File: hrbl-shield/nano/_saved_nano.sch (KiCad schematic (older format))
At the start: 78 parts, among them P1 Digital, P2 Analog, U1 SFH6206-3T, U10 SFH6206-3T, U11 SFH6206-3T, U12 SFH6206-3T, U13 SFH6206-3T, U14 SFH6206-3T, U15 IFX27001TFV50ATMA1CT-ND, U16 SFH6206-3T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

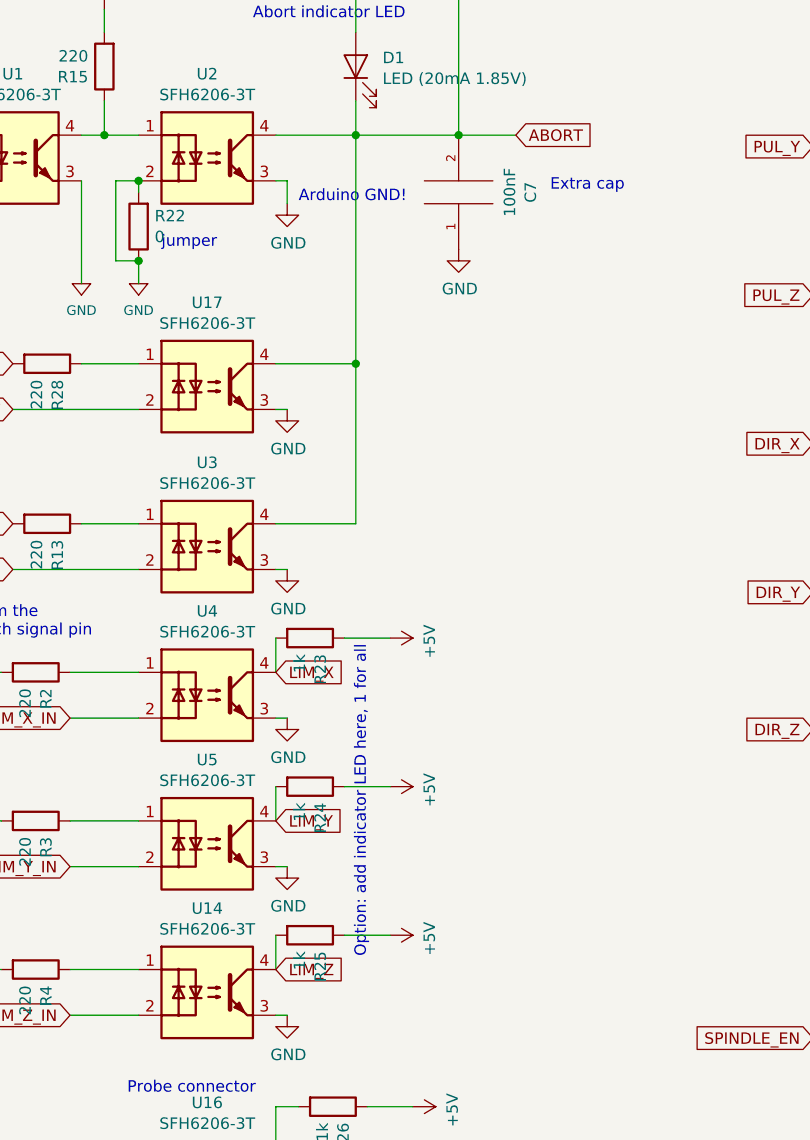
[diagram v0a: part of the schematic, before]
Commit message: Added serial pins and more noise protection
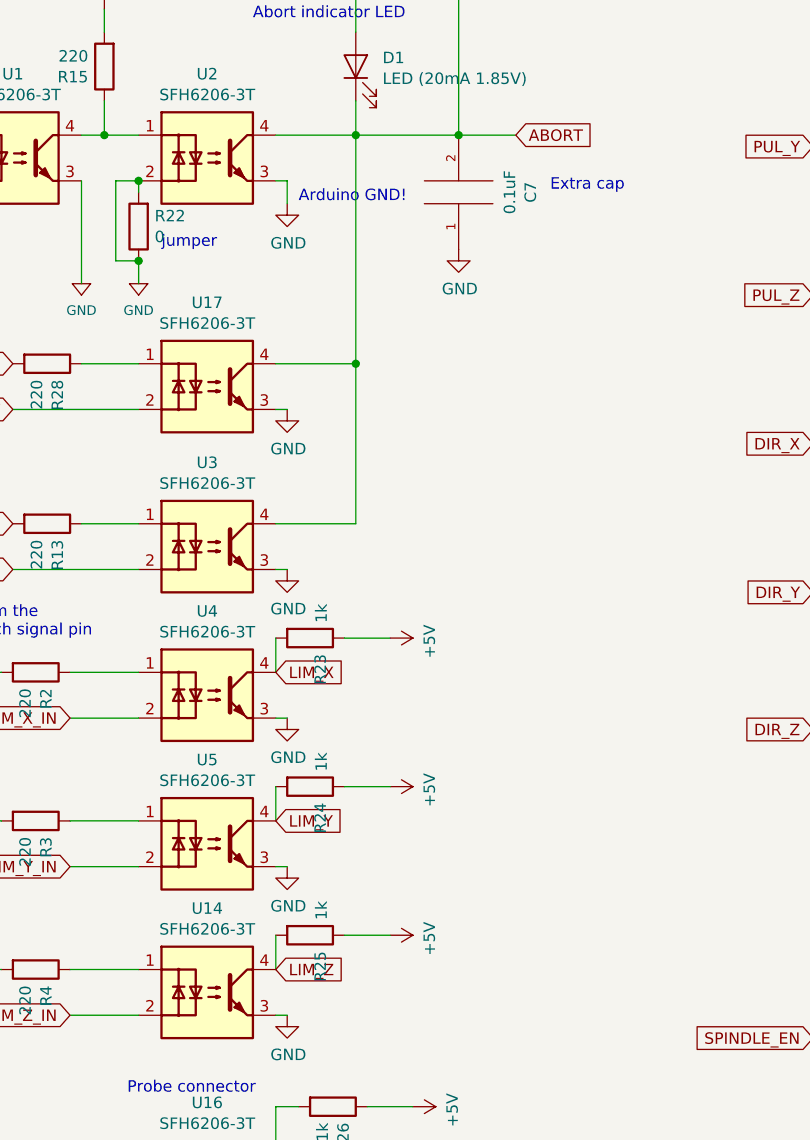
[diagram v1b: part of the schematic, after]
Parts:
- C7: value 100nF -> 0.1uF
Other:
- note removed: "Option: add indicator LED here, 1 for all"
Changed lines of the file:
@@
 PROBE
 $Bitmap
-Pos 11750 1650
+Pos 8300 2400
 Scale 1.000000
 Data
@@
 P 2500 5050
 F 0 "R25" H 2570 5096 50  0000 L CNN
-F 1 "1k" H 2570 5005 50  0000 L CNN
+F 1 "1k" H 2350 5100 50  0000 L CNN
 F 2 "Resistor_SMD:R_1206_3216Metric_Pad1.42x1.75mm_HandSolder" V 2430 5050 50  0001 C CNN
 F 3 "~" H 2500 5050 50  0001 C CNN
@@
 P 2500 4400
 F 0 "R24" H 2570 4446 50  0000 L CNN
-F 1 "1k" H 2570 4355 50  0000 L CNN
+F 1 "1k" H 2350 4450 50  0000 L CNN
 F 2 "Resistor_SMD:R_1206_3216Metric_Pad1.42x1.75mm_HandSolder" V 2430 4400 50  0001 C CNN
 F 3 "~" H 2500 4400 50  0001 C CNN
@@
 P 2500 3750
 F 0 "R23" H 2570 3796 50  0000 L CNN
-F 1 "1k" H 2570 3705 50  0000 L CNN
+F 1 "1k" H 2350 3800 50  0000 L CNN
 F 2 "Resistor_SMD:R_1206_3216Metric_Pad1.42x1.75mm_HandSolder" V 2430 3750 50  0001 C CNN
 F 3 "~" H 2500 3750 50  0001 C CNN
@@
 Wire Wire Line
 	13850 8800 14000 8800
-Text Notes 2750 5150 1    50   ~ 0
-Option: add indicator LED here, 1 for all
 Text Notes 8800 6450 0    50   ~ 0
 Diode for reverse voltage protection of the elektronics\nNot the motors and sensors.
@@
 P 3150 1800
 F 0 "C7" V 2835 1800 50  0000 C CNN
-F 1 "100nF" V 2926 1800 50  0000 C CNN
+F 1 "0.1uF" V 2926 1800 50  0000 C CNN
 F 2 "Capacitor_SMD:C_1206_3216Metric_Pad1.42x1.75mm_HandSolder" H 3150 1800 50  0001 C CNN
 F 3 "" H 3150 1800 50  0001 C CNN
